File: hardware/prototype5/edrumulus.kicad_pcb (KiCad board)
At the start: 2 copper layers, 65 x 56.5 mm, 94 parts, among them J1 Trigger Connector, J2 Raspberry Pi GPIO pins, U1 ESP32-WROOM-32U, U2 AMS1117-3.3, U3 MCP1754S-3302xMB

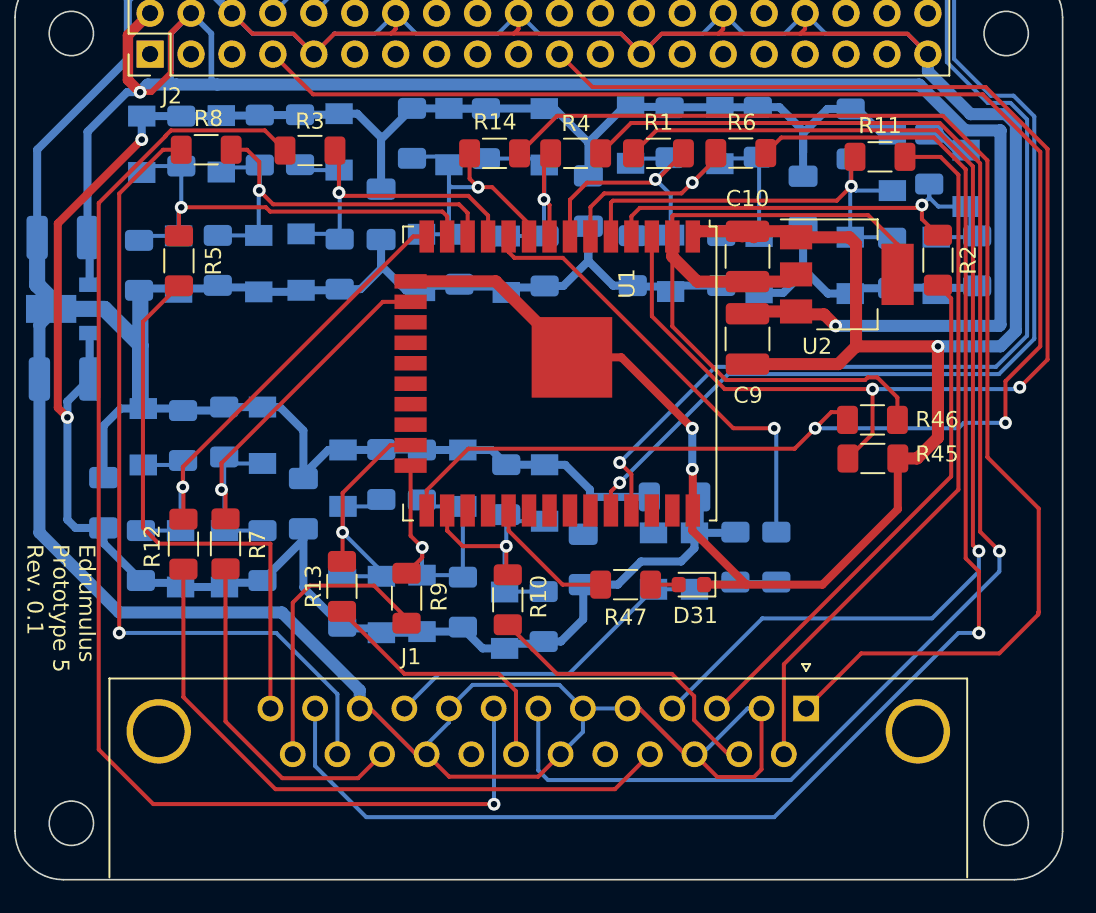
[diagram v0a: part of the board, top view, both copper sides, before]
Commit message: change resistor size from 1206 to 0603 for prototype 5
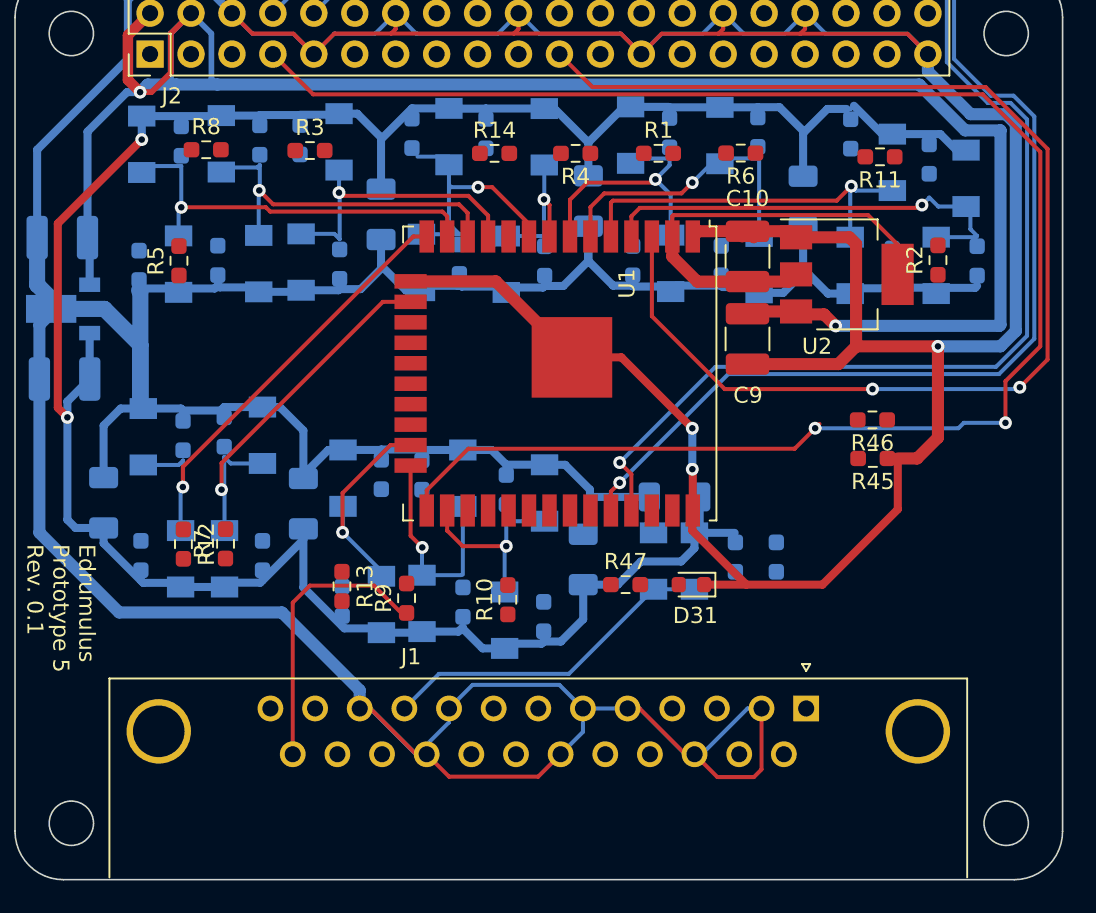
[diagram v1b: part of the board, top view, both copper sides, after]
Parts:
- R1, R10, R11, R12, R13, R14, R15, R16, R17, R18, R19, R2, R20, R21, R22, R23, R24, R25, R26, R27, R28, R29, R3, R30, R31, R32, R33, R34, R35, R36, R37, R38, R39, R4, R40, R41, R42, R43, R44, R45, R46, R47, R5, R6, R7, R8, R9: footprint Resistor_SMD:R_1206_3216Metric_Pad1.30x1.75mm_HandSolder -> Resistor_SMD:R_0603_1608Metric_Pad0.98x0.95mm_HandSolder
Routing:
- net CRASH1-TIP: track 93.5 -> 0.00 mm, vias 1 -> 0
- net HI-HAT-TIP: track 89.2 -> 0.00 mm, vias 1 -> 0
- net HI-HAT-RING: track 79.7 -> 0.00 mm, vias 1 -> 0
- net KICK-TIP: track 77.5 -> 0.00 mm
- net SNARE-RING: track 70.4 -> 0.00 mm, vias 1 -> 0
- net RIDE-TIP: track 51.1 -> 0.00 mm, vias 1 -> 0
- net TOM1-TIP: track 44.2 -> 0.00 mm
- net TOM2-TIP: track 40.2 -> 0.00 mm
- net CRASH1-RING: track 34.5 -> 0.00 mm
- net SNARE-TIP: track 32.7 -> 0.00 mm
- net GPIO25: track 28.5 -> 0.00 mm, vias 1 -> 0
- net ESP32-3V3: track 50.5 -> 27.6 mm
- net RIDE-RING: track 21.3 -> 0.00 mm
- net TOM1-RING: track 18.6 -> 0.00 mm
- net TOM3-TIP: track 16.8 -> 0.00 mm
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
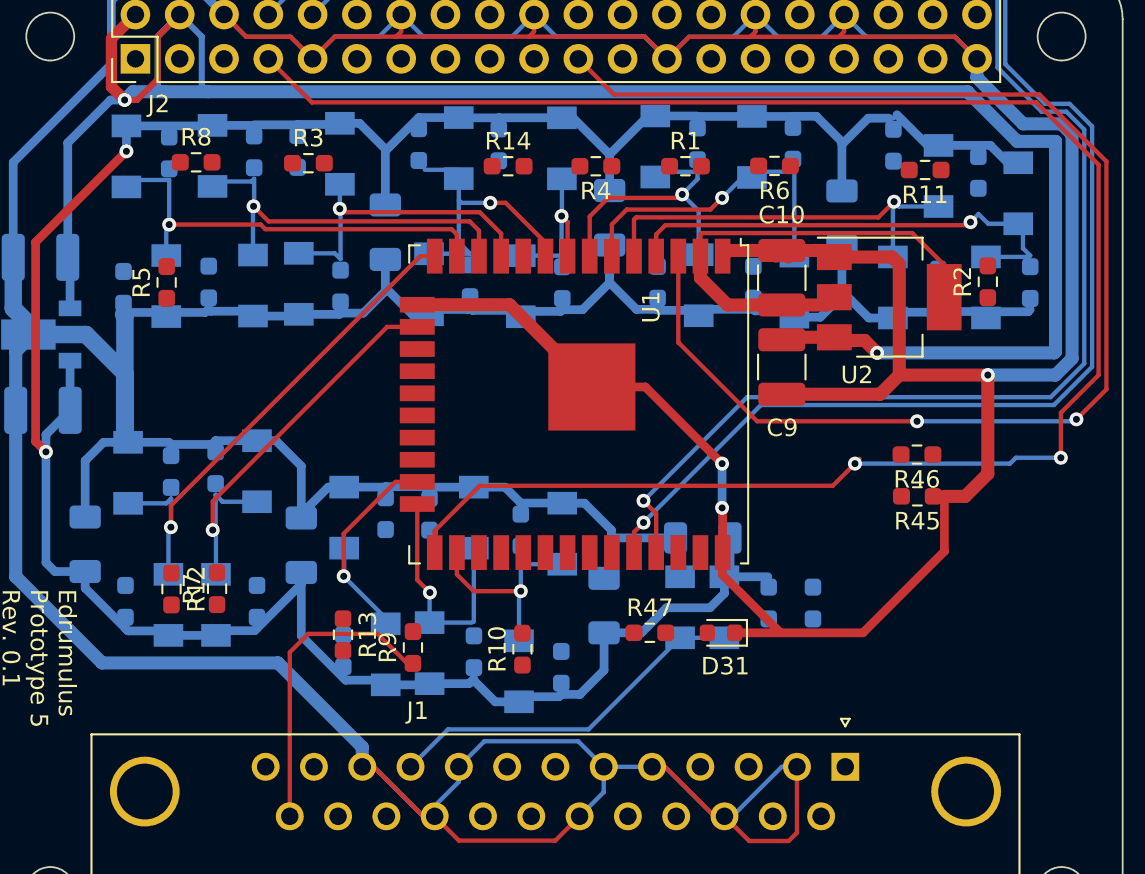
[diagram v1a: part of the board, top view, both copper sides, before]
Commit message: use BAV99 instead of BAT85 diodes
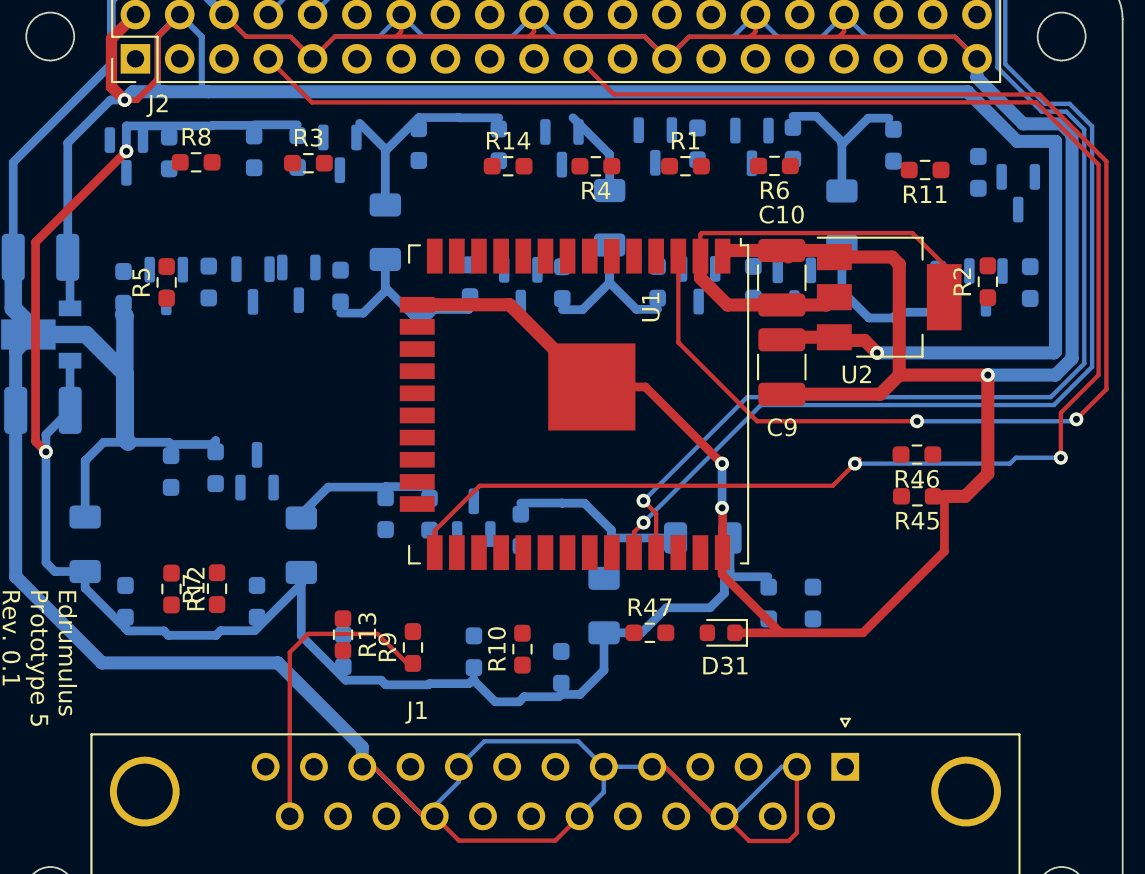
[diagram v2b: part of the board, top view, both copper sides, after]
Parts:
- removed D16, D17, D18, D19, D20, D21, D22, D23, D24, D25, D26, D27, D28, D29, D30: BAT85, Diode_SMD:D_MiniMELF
- D1, D10, D11, D12, D13, D14, D15, D2, D3, D4, D5, D6, D7, D8, D9: value BAT85 -> BAV99; footprint Diode_SMD:D_MiniMELF -> Package_TO_SOT_SMD:SOT-23
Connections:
- D1 pad 1: GPIO35 -> CRASH1-SLEEVE
- D1 pad 2: CRASH1-SLEEVE -> 3V3
- D10 pad 1: 3V3 -> CRASH1-SLEEVE
- D10 pad 2: GPIO35 -> 3V3
- D11 pad 1: 3V3 -> CRASH1-SLEEVE
- D11 pad 2: GPIO36 -> 3V3
- D12 pad 1: 3V3 -> CRASH1-SLEEVE
- D12 pad 2: GPIO26 -> 3V3
- D13 pad 1: 3V3 -> CRASH1-SLEEVE
- D13 pad 2: GPIO32 -> 3V3
- D14 pad 1: 3V3 -> CRASH1-SLEEVE
- D14 pad 2: GPIO14 -> 3V3
- D15 pad 1: 3V3 -> CRASH1-SLEEVE
- D15 pad 2: GPIO34 -> 3V3
- D2 pad 1: GPIO36 -> CRASH1-SLEEVE
- D2 pad 2: CRASH1-SLEEVE -> 3V3
- D3 pad 1: GPIO26 -> CRASH1-SLEEVE
- D3 pad 2: CRASH1-SLEEVE -> 3V3
- D4 pad 1: GPIO32 -> CRASH1-SLEEVE
- D4 pad 2: CRASH1-SLEEVE -> 3V3
- D5 pad 1: GPIO14 -> CRASH1-SLEEVE
- D5 pad 2: CRASH1-SLEEVE -> 3V3
- D6 pad 1: GPIO34 -> CRASH1-SLEEVE
- D6 pad 2: CRASH1-SLEEVE -> 3V3
- D7 pad 1: GPIO13 -> CRASH1-SLEEVE
- D7 pad 2: CRASH1-SLEEVE -> 3V3
- D8 pad 1: GPIO27 -> CRASH1-SLEEVE
- D8 pad 2: CRASH1-SLEEVE -> 3V3
- D9 pad 1: GPIO2 -> CRASH1-SLEEVE
- D9 pad 2: CRASH1-SLEEVE -> 3V3
- R16 pad 1: GPIO36 -> Net-(R16-Pad1)
- R18 pad 1: GPIO32 -> Net-(R18-Pad1)
- R20 pad 1: GPIO34 -> Net-(R20-Pad1)
- R22 pad 1: GPIO27 -> Net-(R22-Pad1)
- R23 pad 1: GPIO2 -> Net-(R23-Pad1)
- R25 pad 2: GPIO36 -> Net-(R16-Pad1)
- R27 pad 2: GPIO32 -> Net-(R18-Pad1)
- R29 pad 2: GPIO34 -> Net-(R20-Pad1)
- R31 pad 2: GPIO27 -> Net-(R22-Pad1)
- R32 pad 2: GPIO2 -> Net-(R23-Pad1)
- R34 pad 1: GPIO12 -> Net-(R34-Pad1)
- R35 pad 1: GPIO15 -> Net-(R35-Pad1)
- R36 pad 1: GPIO33 -> Net-(R36-Pad1)
- R37 pad 2: HI-HAT-CONTROL-TIP -> Net-(R37-Pad2)
- R38 pad 2: GPIO12 -> Net-(R34-Pad1)
- R39 pad 2: GPIO15 -> Net-(R35-Pad1)
- R40 pad 2: GPIO33 -> Net-(R36-Pad1)
- R42 pad 1: GPIO39 -> Net-(R42-Pad1)
- R44 pad 2: GPIO39 -> Net-(R42-Pad1)
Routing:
- net CRASH1-SLEEVE: track 480.4 -> 428.3 mm
- net GPIO12: track 29.3 -> 0.00 mm, vias 1 -> 0
- net 3V3: track 156.3 -> 128.3 mm
- net GPIO36: track 27.4 -> 0.00 mm, vias 1 -> 0
- net GPIO14: track 25.0 -> 0.00 mm, vias 1 -> 0
- net GPIO13: track 24.8 -> 0.00 mm, vias 1 -> 0
- net GPIO39: track 23.3 -> 0.00 mm, vias 1 -> 0
- net GPIO27: track 21.9 -> 0.00 mm, vias 1 -> 0
- net HI-HAT-CONTROL-TIP: track 21.1 -> 0.00 mm
- net GPIO34: track 18.4 -> 0.00 mm, vias 1 -> 0
- net GPIO26: track 18.0 -> 0.00 mm, vias 1 -> 0
- net GPIO35: track 16.2 -> 0.00 mm, vias 1 -> 0
- net GPIO33: track 15.6 -> 0.00 mm, vias 1 -> 0
- net GPIO2: track 13.8 -> 0.00 mm, vias 1 -> 0
- net GPIO15: track 13.2 -> 0.00 mm, vias 1 -> 0
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
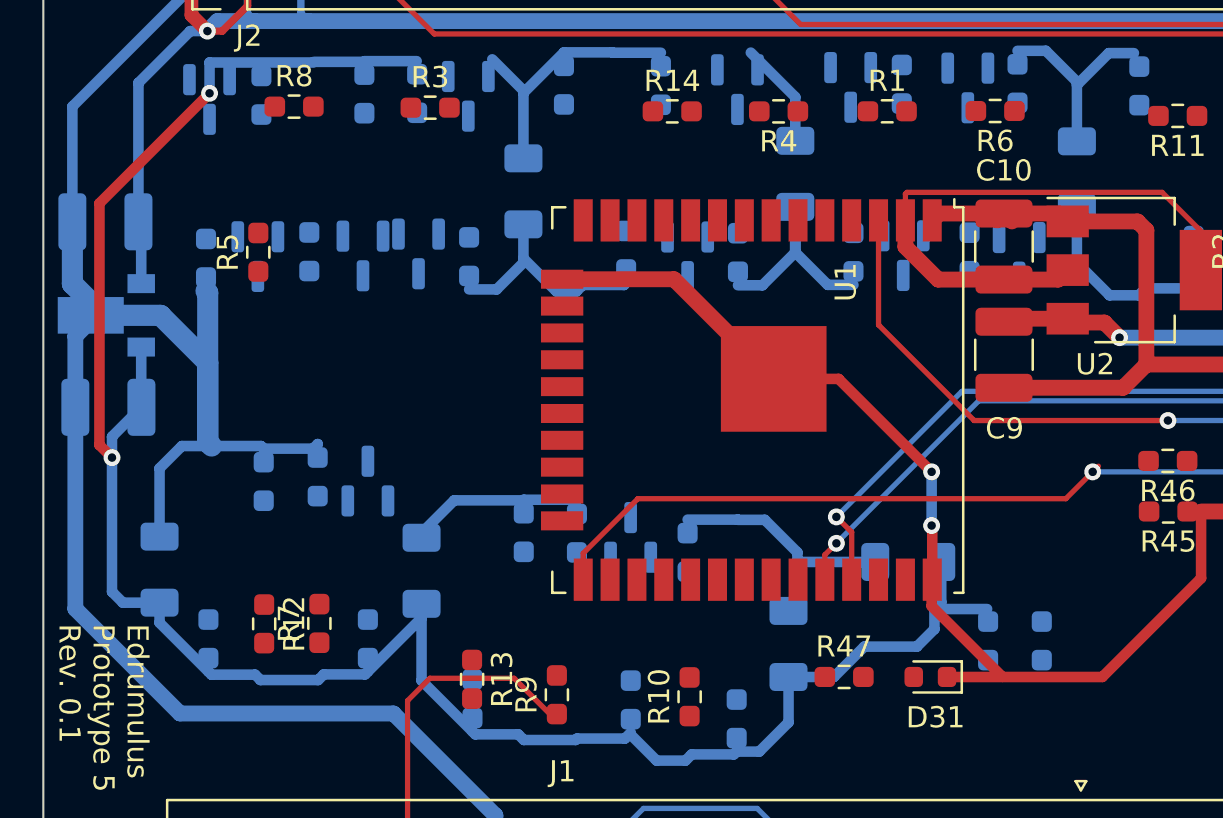
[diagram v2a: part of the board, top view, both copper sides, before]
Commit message: use 0603 for the caps for prototype 5
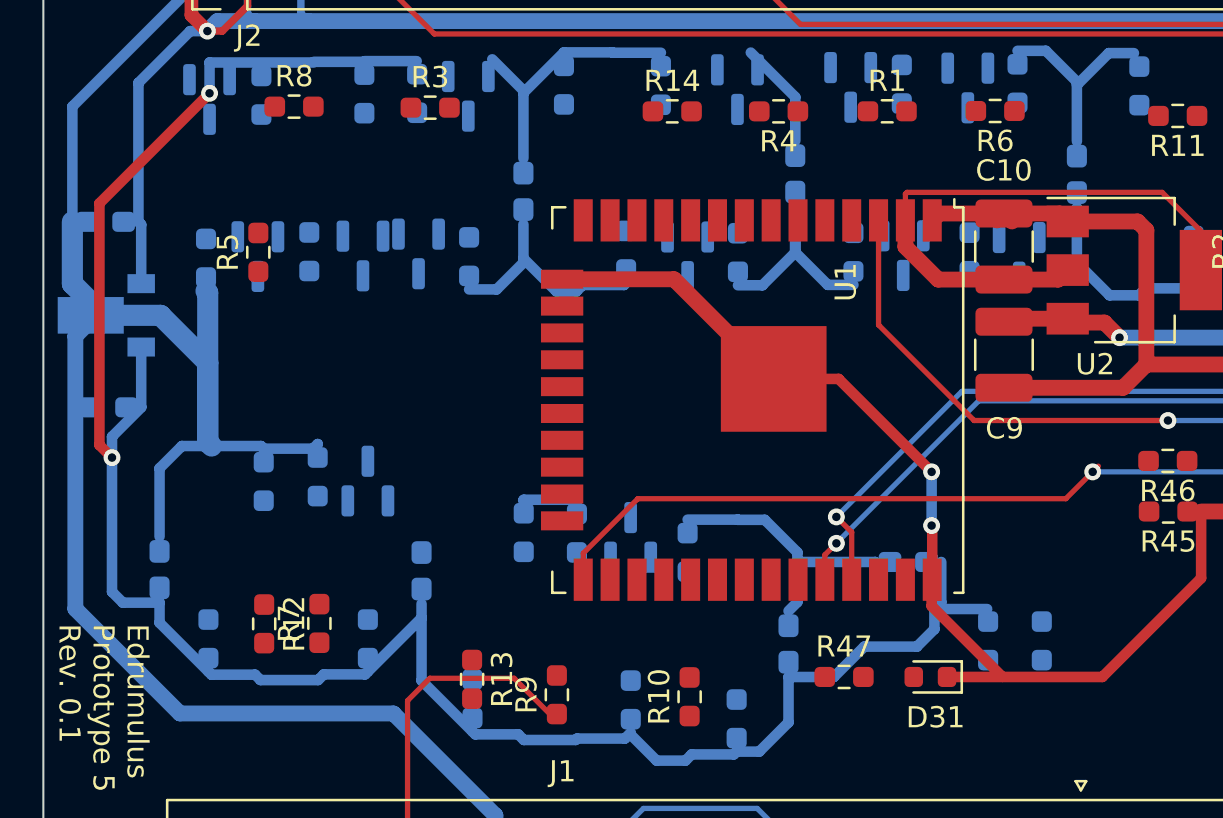
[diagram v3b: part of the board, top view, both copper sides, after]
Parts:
- C1, C2, C3, C4, C5, C6, C7: footprint Capacitor_SMD:C_1206_3216Metric_Pad1.33x1.80mm_HandSolder -> Capacitor_SMD:C_0603_1608Metric_Pad1.08x0.95mm_HandSolder
- C11, C8: footprint Capacitor_SMD:C_1210_3225Metric_Pad1.33x2.70mm_HandSolder -> Capacitor_SMD:C_0603_1608Metric_Pad1.08x0.95mm_HandSolder
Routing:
- net CRASH1-SLEEVE: track 428.3 -> 422.9 mm
